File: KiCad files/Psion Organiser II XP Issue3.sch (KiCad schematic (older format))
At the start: 75 parts, among them X1 LM324

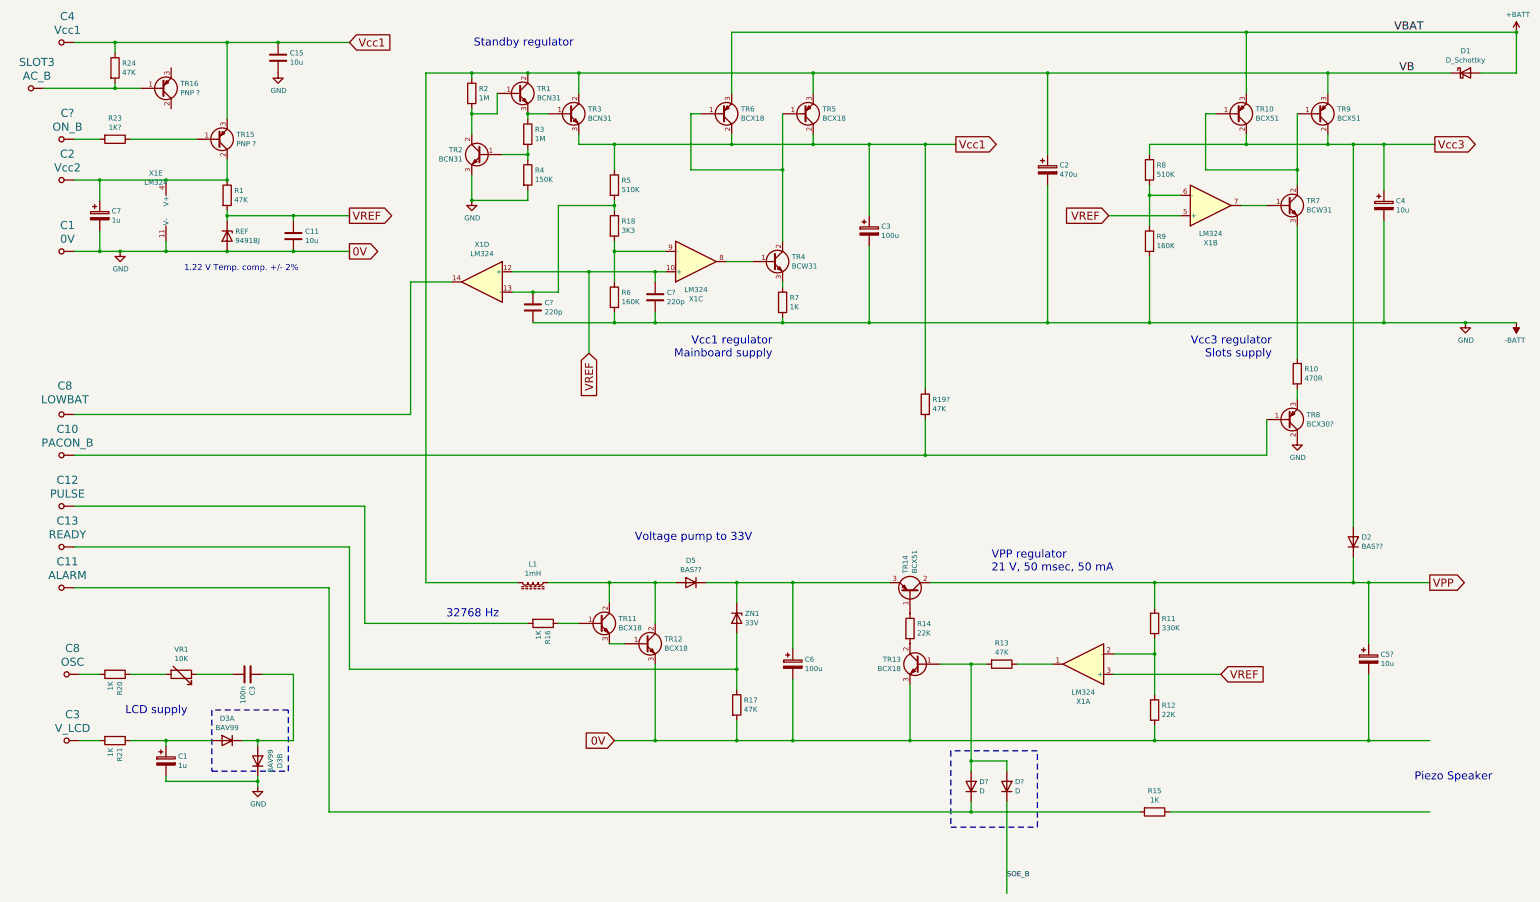
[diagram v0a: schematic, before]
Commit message: updated Power/Standby control
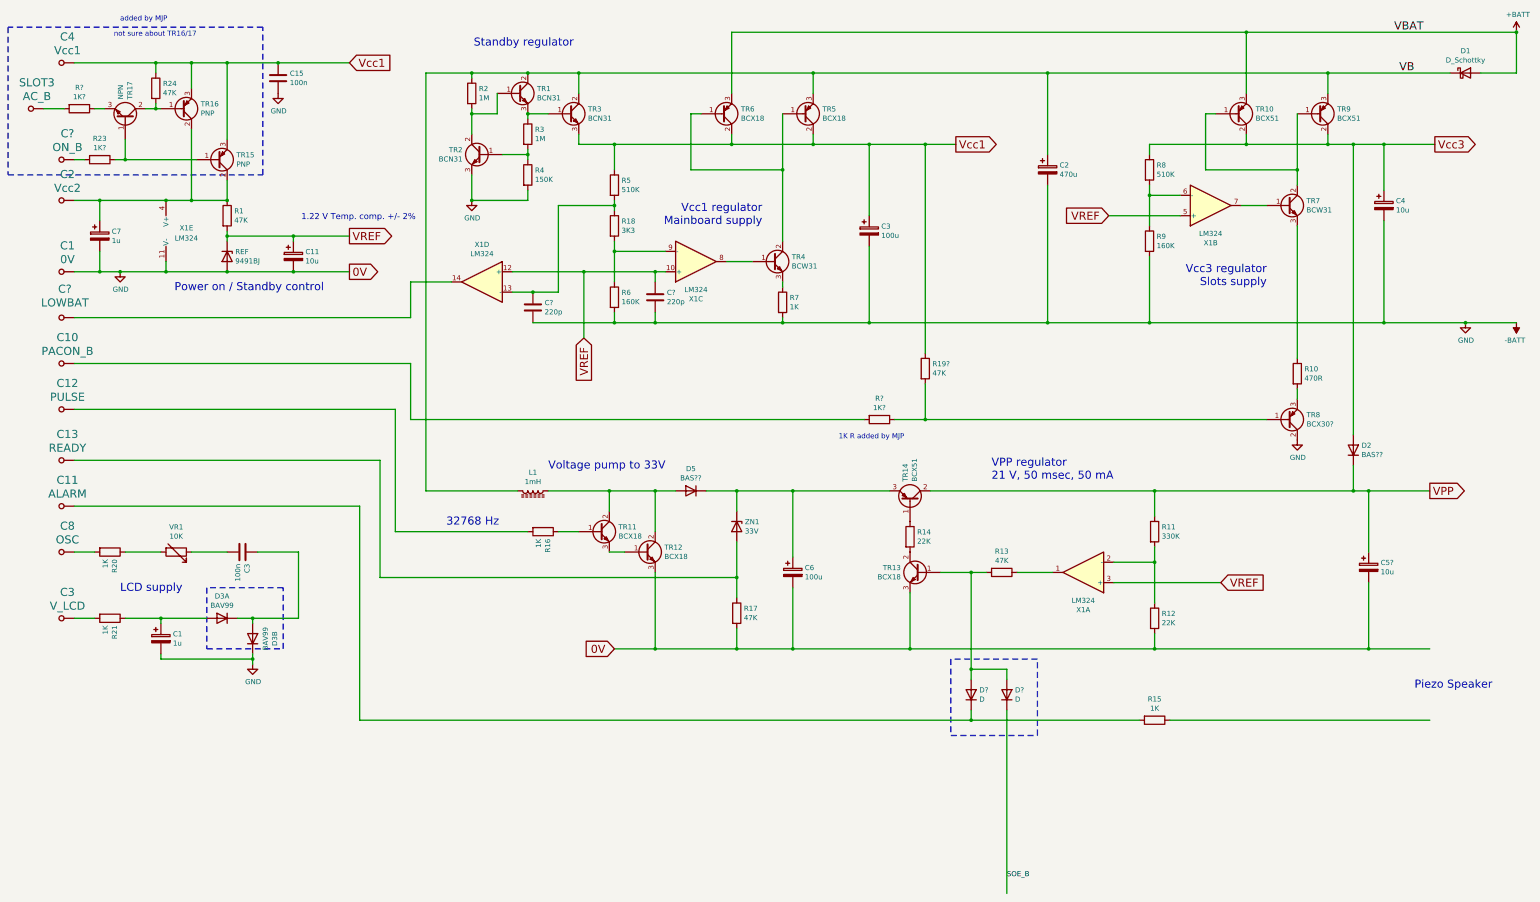
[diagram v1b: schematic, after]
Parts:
- removed C11: 10u, symbol Device:C
- added C11: 10u, symbol Device:CP
- added R? (x2): 1K?, symbol Device:R
- added TR17: NPN, symbol Device:Q_NPN_BCE
- C15: value 10u -> 100n
- TR15, TR16: value PNP ? -> PNP
- renumbered C8 to C?
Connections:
- net -BATT: now also C11.2
- net VREF: now also C11.1
- net Vcc1: now also TR16.3 (E)
- net at C2.~, C7.1, R1.1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: now also TR16.2 (C)
- net at R19?.2, TR8.1 (B): now also R?.1; no longer C10.~
- net at R23.1, TR15.1 (B): now also TR17.1 (B)
- net at R24.2, TR16.1 (B): now also TR17.2 (C); no longer SLOT3.~
- new net: R?.1, TR17.3 (E)
- new net: R?.2, SLOT3.~
- new net: C10.~, R?.2
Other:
- note added: "1K R added by MJP"
- note added: "Power on / Standby control"
- note added: "added by MJP"
- note added: "not sure about TR16/17"
- moved on the sheet: C1, C10, C11, C12, C13, C15, C2, C3, C4, C5?, C6, C7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

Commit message: update to power control
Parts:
- removed TR17: NPN, symbol Device:Q_NPN_BCE
- added CN?: AC, symbol Martins_Library:Conn_psion
- added R?: 47K, symbol Device:R
- gave numbers to parts that had none: 1
- renumbered C1 to CN1, C10 to CN10, C11 to CN11, C12 to CN12, C13 to CN13, C2 to CN2, C3 to CN3, C4 to CN4, C8 to CN8
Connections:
- net -BATT: now also R?.2
- net Vcc1: no longer TR16.3 (E)
- net at R24.2, TR16.1 (B): now also R?.1
- net at C7.1, CN2.~, R1.1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: no longer TR16.2 (C)
- net at CN?.~, R23.2: now also TR16.3 (E)
- new net: CN?.~, R?.1, TR16.2 (C)
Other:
- note added: "contrast wheel"
- note added: "not sure about TR16"
- note removed: "not sure about TR16/17"
- moved on the sheet: C15, CN4, CN?, R23, R24, R?, SLOT3, TR15, TR16

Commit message: updates to power PCB
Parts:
- removed CN1: 0V, symbol Martins_Library:Conn_psion
- removed CN10: PACON_B, symbol Martins_Library:Conn_psion
- removed CN11: ALARM, symbol Martins_Library:Conn_psion
- removed CN12: PULSE, symbol Martins_Library:Conn_psion
- removed CN13: READY, symbol Martins_Library:Conn_psion
- removed CN2: Vcc2, symbol Martins_Library:Conn_psion
- removed CN3: V_LCD, symbol Martins_Library:Conn_psion
- removed CN4: Vcc1, symbol Martins_Library:Conn_psion
- removed CN8: OSC, symbol Martins_Library:Conn_psion
- removed CN?: LOWBAT, symbol Martins_Library:Conn_psion
- removed CN?: AC, symbol Martins_Library:Conn_psion
- removed CN?: ON_B, symbol Martins_Library:Conn_psion
- removed R?: 47K, symbol Device:R
- removed R?: 1K?, symbol Device:R
- removed SLOT3: AC_B, symbol Martins_Library:Conn_psion
- added C13 (x2): 33p, symbol Device:C
- added C14: 20p, symbol Device:C_Variable
- added Mainboard: ribbon cable, symbol Connector:Conn_01x27_Female
- added R?: 47K, symbol Device:R
- added R?: 1M?, symbol Device:R
- added R?: 150K, symbol Device:R
- added SLOT1(B), SLOT2(C): Conn_02x08_Male, symbol Connector:Conn_01x16_Male
- added TOPSLOT(D): Conn_02x08_Female, symbol Connector:Conn_01x16_Female
- added U1: 74LS132, symbol 74xx:74LS132
- added Y?: Crystal, symbol Device:Crystal
- R22?: renamed from R?; value 1K? -> 47K?
- R23: value 1K? -> 47K?
- gave numbers to parts that had none: 1
- renumbered C3 to C8
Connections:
- net -BATT: now also C13.2, C13.2, C14.2, Mainboard.1 (Pin_1), SLOT1(B).13 (Pin_13), SLOT2(C).13 (Pin_13), TOPSLOT(D).9 (Pin_9), U1.10, U1.12, U1.13, U1.7 (GND), U1.9; no longer TR13.3 (E)
- net SOE_B: now also Mainboard.15 (Pin_15), SLOT1(B).11 (Pin_11), SLOT2(C).11 (Pin_11), TOPSLOT(D).15 (Pin_15)
- net VB: now also TOPSLOT(D).11 (Pin_11)
- net Vcc1: now also Mainboard.4 (Pin_4), U1.1, U1.14 (VCC), U1.4
- net Vcc3: now also R?.1, SLOT1(B).15 (Pin_15), SLOT2(C).15 (Pin_15), TOPSLOT(D).13 (Pin_13)
- net LOWBAT: now reaches X1.14
- net LOWBAT: now also Mainboard.6 (Pin_6)
- net READY: now reaches R17.1, ZN1.2 (A)
- net READY: now also Mainboard.13 (Pin_13)
- net ALARM: now reaches D?.1 (K), R15.2
- net ALARM: now also Mainboard.11 (Pin_11)
- net OSC: now reaches R20.2
- net OSC: now also Mainboard.8 (Pin_8)
- net V_LCD: now reaches R21.2
- net V_LCD: now also Mainboard.3 (Pin_3)
- net Vcc2: now reaches C7.1, R1.1, TR15.2 (C), X1.4 (V+)
- net Vcc2: now also Mainboard.2 (Pin_2)
- net PULSE: now reaches R16.2
- net PULSE: now also Mainboard.12 (Pin_12)
- net ACN: now reaches TR16.2 (C)
- net ACN: now also Mainboard.5 (Pin_5)
- net PACON_B: now reaches R19?.2, TR8.1 (B)
- net PACON_B: now also Mainboard.10 (Pin_10)
- net at R10.2, TR8.3 (E): now also TR13.3 (E)
- net at R22?.1, TR16.1 (B): no longer R24.2
- net AC_B: now reaches R22?.2
- net AC_B: now also R24.2, TOPSLOT(D).14 (Pin_14)
- net Piezo(+): now reaches R15.1
- net ON_B: now reaches R23.2, TR16.3 (E)
- net ON_B: now also Mainboard.7 (Pin_7)
- net VPP renamed Vpp
- net Vpp: now also SLOT1(B).16 (Pin_16), SLOT2(C).16 (Pin_16)
- new net: C13.1, C14.1, R?.1, R?.2, Y?.1
- new net: C13.1, R?.2, U1.5, Y?.2
- new net: R?.1, U1.2, U1.6
- new net CLK: U1.3
- new net SCK: Mainboard.19 (Pin_19), SLOT1(B).10 (Pin_10), SLOT2(C).10 (Pin_10), TOPSLOT(D).10 (Pin_10)
- new net SD0: Mainboard.27 (Pin_27), SLOT1(B).2 (Pin_2), SLOT2(C).2 (Pin_2), TOPSLOT(D).2 (Pin_2)
- new net SD1: Mainboard.26 (Pin_26), SLOT1(B).1 (Pin_1), SLOT2(C).1 (Pin_1), TOPSLOT(D).4 (Pin_4)
- new net SD2: Mainboard.25 (Pin_25), SLOT1(B).4 (Pin_4), SLOT2(C).4 (Pin_4), TOPSLOT(D).6 (Pin_6)
- new net SD3: Mainboard.24 (Pin_24), SLOT1(B).3 (Pin_3), SLOT2(C).3 (Pin_3), TOPSLOT(D).8 (Pin_8)
- new net SD4: Mainboard.23 (Pin_23), SLOT1(B).6 (Pin_6), SLOT2(C).6 (Pin_6), TOPSLOT(D).7 (Pin_7)
- new net SD5: Mainboard.22 (Pin_22), SLOT1(B).5 (Pin_5), SLOT2(C).5 (Pin_5), TOPSLOT(D).5 (Pin_5)
- new net SD6: Mainboard.21 (Pin_21), SLOT1(B).8 (Pin_8), SLOT2(C).8 (Pin_8), TOPSLOT(D).3 (Pin_3)
- new net SD7: Mainboard.20 (Pin_20), SLOT1(B).7 (Pin_7), SLOT2(C).7 (Pin_7), TOPSLOT(D).1 (Pin_1)
- new net SMR: Mainboard.18 (Pin_18), SLOT1(B).9 (Pin_9), SLOT2(C).9 (Pin_9), TOPSLOT(D).16 (Pin_16)
- new net SPGM_B: Mainboard.14 (Pin_14), R?.2, SLOT1(B).14 (Pin_14), SLOT2(C).14 (Pin_14)
- new net SS1_B: Mainboard.16 (Pin_16), SLOT1(B).12 (Pin_12)
- new net SS2_B: Mainboard.17 (Pin_17), SLOT2(C).12 (Pin_12)
- new net SS3_B: Mainboard.9 (Pin_9), TOPSLOT(D).12 (Pin_12)
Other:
- note added: "1024 Hz"
- note added: "Clock moved from mainboard\nat Issue 3 PCB"
- note added: "From TOPSLOT"
- note added: "LCD contrast"
- note added: "confident"
- note added: "diode supplies Vpp from Vcc3\nwhen voltage pump is off"
- note added: "diodes ensure ALARM and SOE_B \nare high for VPP on"
- note added: "shared \npackage"
- note added: "unsure"
- note added: "unsure about pin numbers \nNAND gate type\nand component values"
- note removed: "1K R added by MJP"
- note removed: "added by MJP"
- note removed: "not sure about TR16"
- moved on the sheet: C1, C10?, C11, C15, C2, C3, C4, C5?, C6, C7, C8, C?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

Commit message: update components and filenames
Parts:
- removed D1: D_Schottky, symbol Device:D_Schottky
- added D1: BAS16, symbol Device:D
- C1: Max Voltage (none) -> 30 V
- C11: Max Voltage (none) -> 25 V
- C2: Max Voltage (none) -> 16 V
- C3: Max Voltage (none) -> 6V3?
- C4: Max Voltage (none) -> 35 V
- C5: renamed from C5?; Max Voltage (none) -> 25V
- C6: Max Voltage (none) -> 40V
- C7: Max Voltage (none) -> 50 V
- D2, D5: value BAS?? -> BAS16?
- D4A, D4B: renamed from D?; value D -> BAW56
- R22: renamed from R22?; value 47K? -> 47K
- R23: value 47K? -> 47K
- R24?: renamed from R?; value 1M? -> 10M?
- TR1, TR2, TR3: value BCN31 -> BCW31?
- XTAL1: renamed from Y?; value Crystal -> 32768 Hz?
- gave numbers to parts that had none: 1
- renumbered C13 to C12
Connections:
- net +BATT: now also D1.2 (A)
- net VB: now also D1.1 (K)
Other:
- note added: "pullup"
- moved on the sheet: C4, R10, R13, R15, R9, U1C, U1D, XTAL1
